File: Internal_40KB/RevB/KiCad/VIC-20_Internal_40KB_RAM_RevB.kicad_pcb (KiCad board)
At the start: 2 copper layers, 66 x 62.2 mm, 17 parts, among them J1 BLK Decoder, J2 RAM Decoder, J3 Disable/Enable Switch, J4 UD4, J5 UE4, U1 74HCT138, U2 74HCT138, U3 74HCT10, U4 74HCT30, U5 74HCT157, U6 62256

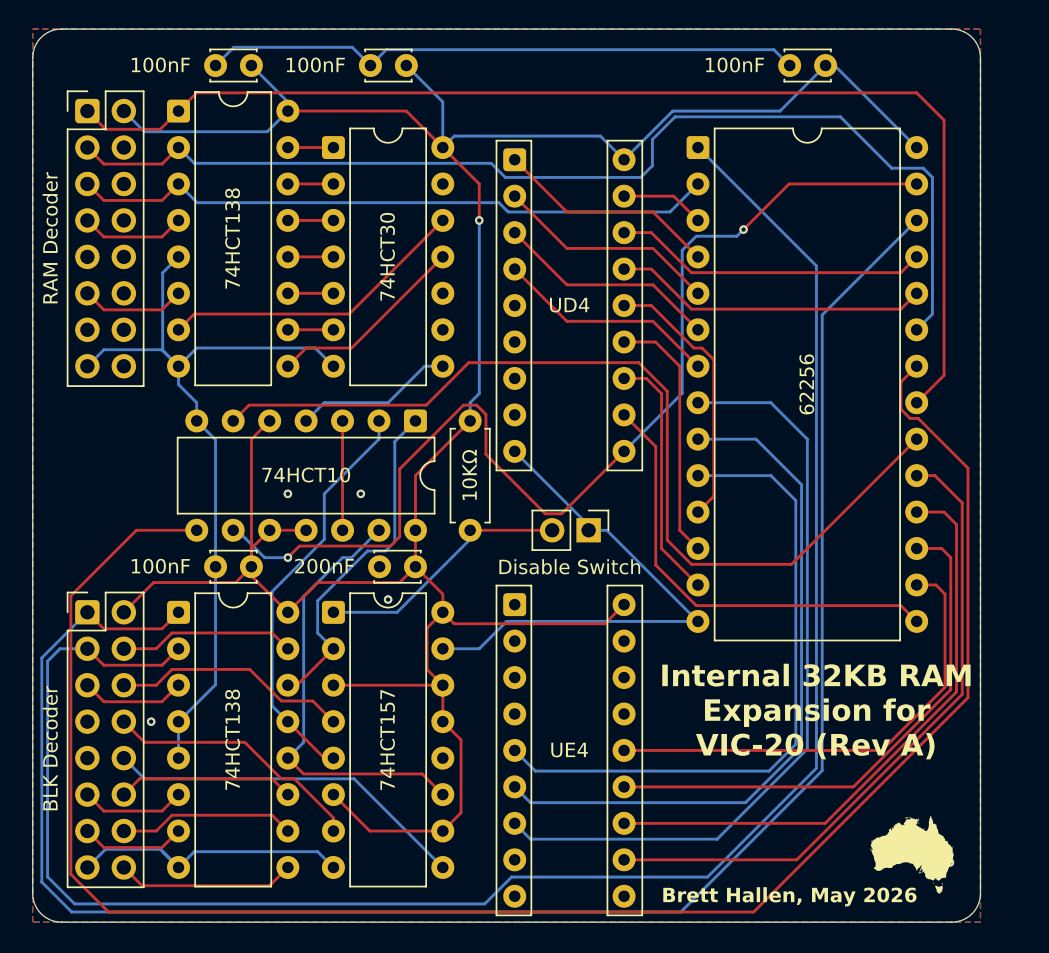
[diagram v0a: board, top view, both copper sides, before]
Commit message: Initial Rev B design
A simple extension of the 32KB expansion by adding a 6264 piggybacked on top of the 62256 and routing the ~BLK5 select to it.
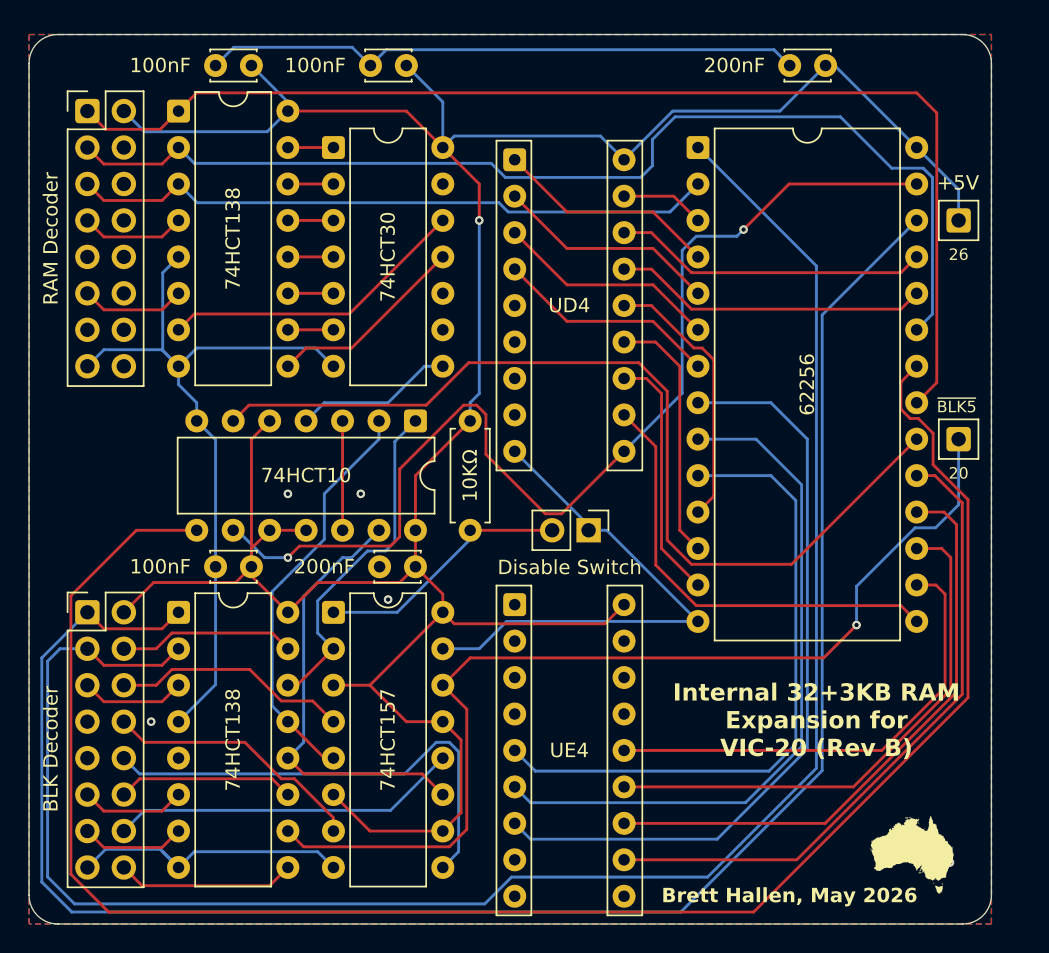
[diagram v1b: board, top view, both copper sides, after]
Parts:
- added J6: 20, Connector_PinHeader_2.54mm:PinHeader_1x01_P2.54mm_Vertical, F.Cu at (131.1, 60.1)
- added J7: 26, Connector_PinHeader_2.54mm:PinHeader_1x01_P2.54mm_Vertical, F.Cu at (131.1, 44.9)
- C3: value 100nF -> 200nF
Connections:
- J1 pad 10: /~{BLK5} -> /~{BLK5_{OUT}}
- U5 pad 12: unconnected-(U5-Zd-Pad12) -> /~{BLK5_{OUT}}
- U5 pad 14: +5V -> /~{BLK5}
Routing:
- net /~{BLK5}: track 12.3 -> 71.5 mm, vias 0 -> 1
- net /~{BLK5_{OUT}}: track 0.00 -> 24.3 mm
- net /~{BLK3_{OUT}}: track 25.4 -> 33.5 mm
- net +5V: track 199.5 -> 205.5 mm
- net GND: track 157.1 -> 153.7 mm
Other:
- board size 66 x 62.2 mm -> 67.1 x 62 mm
- board text added: "+5V"
- board text added: "32KB SRAM (plus optional 6264 SRAM)"
- board text added: "Internal 32+3KB RAM Expansion for VIC-20 (Rev B)"
- board text added: "~{BLK5}"
- board text removed: "26-MAY-2026: Pending testing"
- board text removed: "32KB SRAM"
- board text removed: "Internal 32KB RAM Expansion for VIC-20 (Rev A)"

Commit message: Added +3KB disable switch
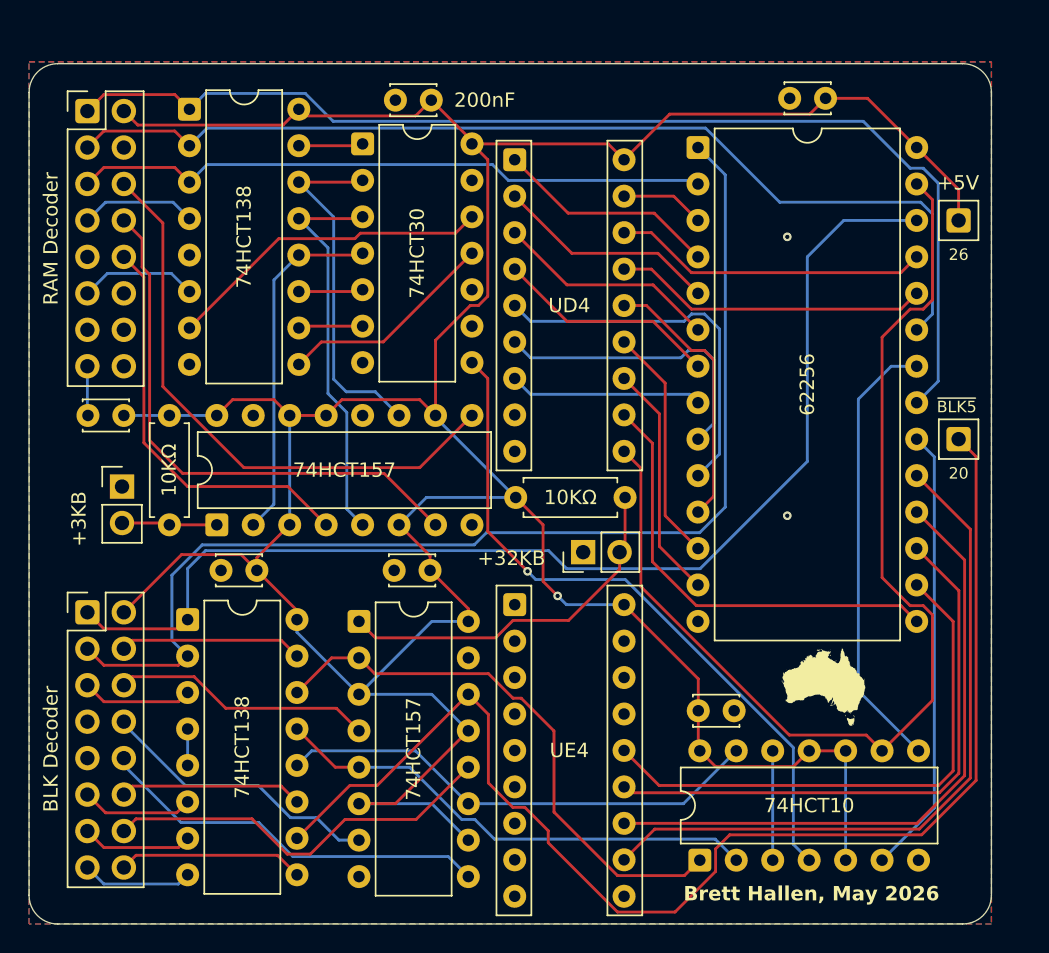
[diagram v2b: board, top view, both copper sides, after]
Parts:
- removed the C2 at (92.6, 34.1)
- added C5: 100nF, Capacitor_THT:C_Disc_D3.0mm_W2.0mm_P2.50mm, F.Cu at (72.9, 58.5)
- added C6: 100nF, Capacitor_THT:C_Disc_D3.0mm_W2.0mm_P2.50mm, F.Cu at (112.9, 79.0)
- added J4: +3KB Disable, Connector_PinHeader_2.54mm:PinHeader_1x02_P2.54mm_Vertical, F.Cu at (72.8, 63.4)
- added R2: 10KΩ, Resistor_THT:R_Axial_DIN0207_L6.3mm_D2.5mm_P7.62mm_Horizontal, F.Cu at (76.1, 58.5)
- added U6: 74HCT157, Package_DIP:DIP-16_W7.62mm, F.Cu at (79.4, 66.1)
- C1: value 100nF -> 200nF
- C2: renamed from C3; value 200nF -> 100nF
- C3: renamed from C5; value 200nF -> 100nF
- moved U3 36.5 mm to (113.0, 89.4), turned to 90 degrees
- moved C1 12.8 mm to (94.3, 36.5)
- moved R1 6.21 mm to (100.2, 64.2), turned to 0 degrees
- moved C2 2.29 mm to (121.8, 36.4)
- moved U5 2.05 mm to (89.5, 39.5)
- moved U4 1.89 mm to (89.3, 72.8)
- moved J3 1.57 mm to (104.9, 68.0), turned to 90 degrees
- moved C3 1.05 mm to (94.2, 69.2)
- moved U1 0.81 mm to (77.3, 72.7)
- moved U2 0.77 mm to (77.5, 37.1)
- moved C4 0.46 mm to (82.2, 69.2)
- renumbered J2 to J1, J1 to J2, J4 to J5, J5 to J6, J6 to J8, U5 to U4, U4 to U5, U6 to U8
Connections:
- J1 pad 12: unconnected-(J2-Pin_12-Pad12) -> /~{RAM3_{OUT}}
- J1 pad 13: unconnected-(J2-Pin_13-Pad13) -> /~{RAM2_{OUT}}
- J1 pad 14: unconnected-(J2-Pin_14-Pad14) -> /~{RAM1_{OUT}}
- J5 pad 5: unconnected-(J4-Pin_5-Pad5) -> /VA0
- J5 pad 6: unconnected-(J4-Pin_6-Pad6) -> /VA1
- J5 pad 7: unconnected-(J4-Pin_7-Pad7) -> /VA2
- J6 pad 5: /VA0 -> unconnected-(J6-Pin_5-Pad5)
- J6 pad 6: /VA1 -> unconnected-(J6-Pin_6-Pad6)
- J6 pad 7: /VA2 -> unconnected-(J6-Pin_7-Pad7)
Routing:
- net GND: track 153.7 -> 13.7 mm, vias 5 -> 2
- net /~{OE}: track 125.7 -> 31.3 mm
- net /CA14: track 130.4 -> 80.2 mm
- net +5V: track 205.5 -> 254.1 mm
- net /CA13: track 127.8 -> 81.5 mm
- net /~{RAM1_{OUT}}: track 0.00 -> 40.6 mm
- net /VA2: track 53.7 -> 13.5 mm
- net /~{RAM2_{OUT}}: track 0.00 -> 38.4 mm
- net /~{RAM_CS}: track 11.1 -> 48.1 mm, vias 0 -> 1
- net /~{CS}: track 64.8 -> 31.4 mm
- net /~{RAM3_{OUT}}: track 0.00 -> 28.6 mm
- net /VA1: track 48.8 -> 20.8 mm
- net /~{RAM2}: track 3.18 -> 27.7 mm
- net /~{RAM1}: track 3.18 -> 24.8 mm
- net /~{RAM3}: track 3.18 -> 24.6 mm
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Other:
- board size 67.1 x 62 mm -> 67.1 x 59.9 mm
- board text added: "+32KB"
- board text added: "+3KB"
- board text removed: "Disable Switch"
